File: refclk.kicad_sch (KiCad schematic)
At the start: 57 parts, among them J10 U.FL-R, Q1 PMOS Si2343DS, Q2 MMBT3904, Q3 PMOS Si2343DS, U14 LP5907MFX-3.3, U16 TLV3501, U18 NC7SV157, U19 74LVC2G14, U20 Si5351A, U21 NC7SV157, U22 SN65LVDS1, X1 TCXO-27M

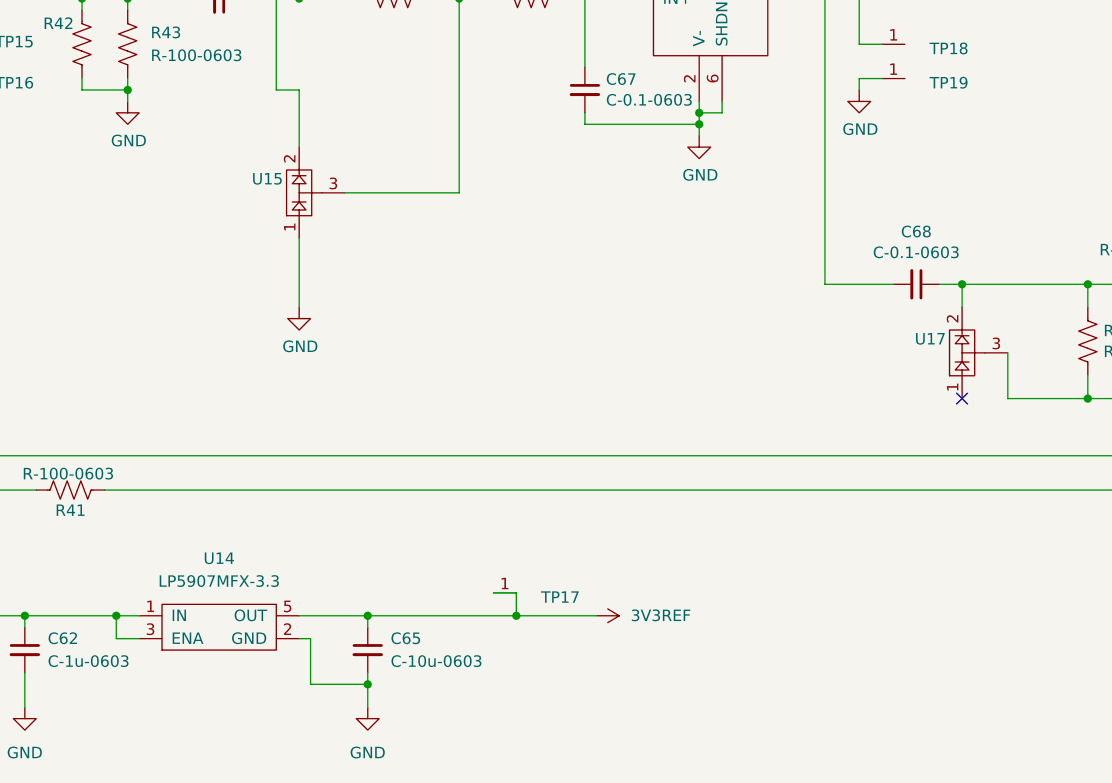
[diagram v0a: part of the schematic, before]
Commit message: Bring over ringof/dev: design + 3D + mechanical/viewer + CI (#58)
* throwaway: exercise design -> dev pipeline (safe to delete)

* Bring over ringof/dev (tranche 2, stage 1): design, library, 3D, board CI & docs

* Bring over ringof/dev (tranche 2, stage 2): mechanical enclosure + 3D viewer

* run_checks: hard-fail the 3D-model check regardless of ENFORCE

* Improved 3D viewer (#59)

* mechanical: give the end plates a Blue soldermask stackup

The end-plate PCBs had no physical stackup, so KiCad exported them with the
default green soldermask. Add a 2-layer stackup with front/back mask set to the
named "Blue" preset, summing to the existing 1.6 mm so board thickness / fit is
unchanged. This makes the plates export blue-dominant so the viewer's soldermask
recolour treats them the same as the main board.

* feat(viewer): part toggles, upright orientation, Turn Island navy, even lighting

Grow the mechanical fit-check viewer into an interactive, correctly-coloured one:

- Part toggles: show/hide enclosure, main board, front/rear end plate. Rebuilt on
  pinned three.js r148 (model-viewer has no per-node visibility API); a checkbox
  flips object.visible on each part's prefixed nodes. Libraries inlined via a
  runtime import map -- no bundler, fully offline.
- Upright orientation (180 deg roll), click-to-set-pivot, and a header showing the
  git hash and branch as links (new --repo-url, fed from the CI environment).
- Board colour: assemble_glb recolours the blue soldermask to the Turn Island navy
  (KiCad's "Blue" preset exports a brighter cornflower); detection targets only the
  matte, blue-dominant mask material. The material is identical on every face, so
  the viewer lighting is set to an orientation-independent rig (soft key + strong
  ambient + damped environment) so every face reads the same navy.
- Checkbox reload-sync: autocomplete="off" + re-apply each box's state on load so
  the model always matches the checkboxes after a refresh.

Colour is applied downstr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
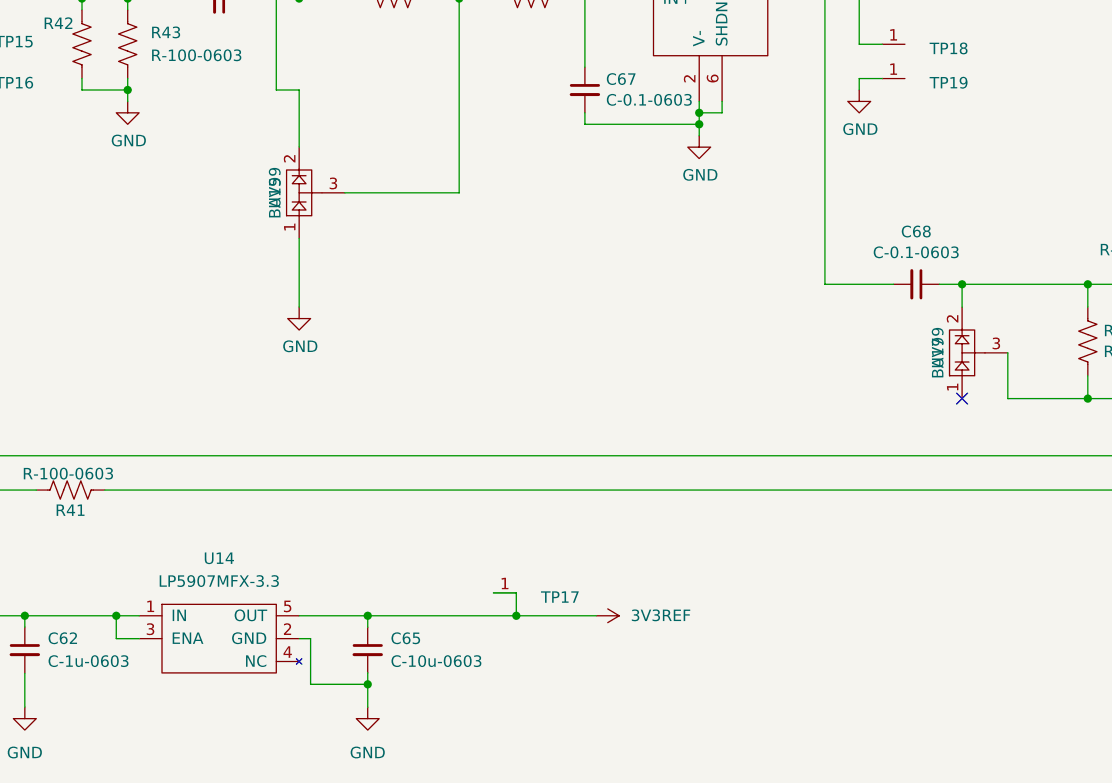
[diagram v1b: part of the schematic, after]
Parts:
- C62, C65: footprint TIS_Footprints:PAD_0603 -> Library:C_0603
- C63, C64, C66, C67, C68, C69, C70, C71, C72, C73, C74, C75, C76: footprint TIS_Footprints:C_0603 -> Library:C_0603
- C78: footprint TIS_Footprints:PAD_0603 -> Library:C_0603; symbol capacitors:C-8.2p-0603 -> Library:C-8.2p-0603
- J10: footprint TIS_Footprints:HRS_U.FL-R-SMT(01) -> Library:HRS_U.FL-R-SMT(01)
- L15, L16, L17: footprint TIS_Footprints:0603 -> Library:0603
- Q1, Q2, Q3: footprint TIS_Footprints:SOT-23 -> Library:SOT-23
- R41, R42, R43, R44, R45, R46, R47, R48, R49, R50, R51, R52, R53, R54, R55, R56, R57, R60: footprint TIS_Footprints:PAD_0603 -> Library:PAD_0603
- R61: footprint TIS_Footprints:PAD_0603 -> Library:PAD_0603; symbol resistors:R-100-0603 -> Library:R-100-0603
- TP15, TP16, TP17, TP18, TP19: footprint TIS_Footprints:TP -> Library:TP
- U14, U22: footprint TIS_Footprints:SOT-23-5 -> Library:SOT-23-5
- U15, U17: value (none) -> BAV99; footprint TIS_Footprints:SOT-23 -> Library:SOT-23
- U16: footprint TIS_Footprints:SOT-23-6 -> Library:SOT-23-6
- U18, U21: footprint TIS_Footprints:SC-70-6 -> Library:SC-70-6
- U19: footprint TIS_Footprints:SC-70-6_rot90 -> Library:SC-70-6_rot90
- U20: footprint TIS_Footprints:MSOP-10_W3mm -> Library:MSOP-10_W3mm
- X1: footprint TIS_Footprints:TCXO-3225 -> Library:TCXO-3225; Comment alternate: C46598427 ±2ppm -> (none)

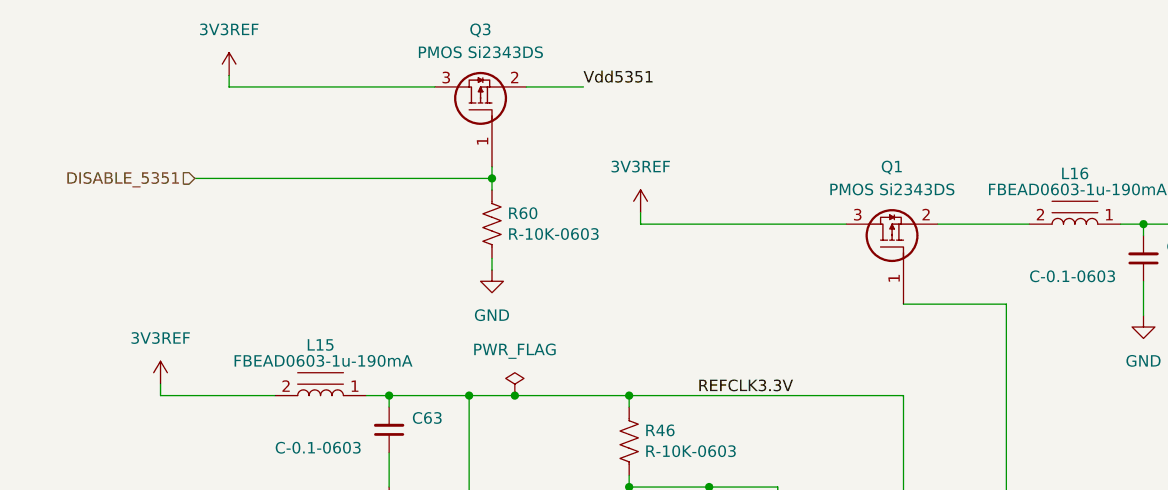
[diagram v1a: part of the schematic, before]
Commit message: Q1/Q3 D/S swap, TP11, TP12 to TPTiny and relocate
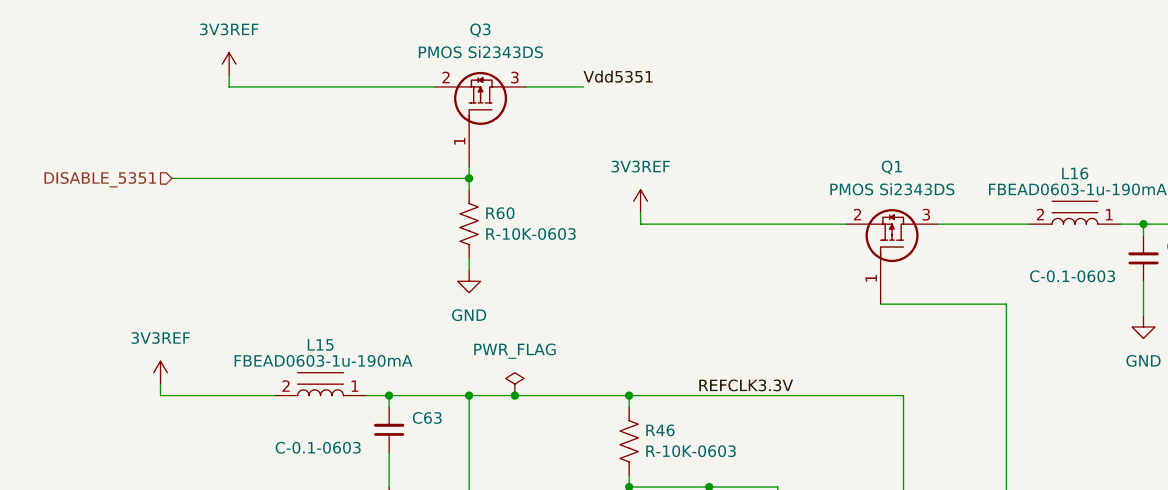
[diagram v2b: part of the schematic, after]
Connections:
- net 3V3REF: now also Q1.2 (S), Q3.2 (S); no longer Q1.3 (D), Q3.3 (D)
- net Vdd5351: now also Q3.3 (D); no longer Q3.2 (S)
- net at L16.2: now also Q1.3 (D); no longer Q1.2 (S)
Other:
- moved on the sheet: Q1, Q3, R60
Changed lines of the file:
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@@
 	)
 	(junction
-		(at 63.5 31.75)
+		(at 60.96 31.75)
 		(diameter 0)
 		(color 0 0 0 0)
@@
 	(wire
 		(pts
-			(xy 63.5 31.75) (xy 63.5 33.02)
+			(xy 60.96 31.75) (xy 60.96 33.02)
 		)
 		(stroke
@@
 	(wire
 		(pts
-			(xy 120.65 45.72) (xy 109.22 45.72)
-		)
-		(stroke
-			(width 0)
-			(type default)
-		)
-	)
-	(wire
-		(pts
 			(xy 146.05 36.83) (xy 146.05 64.77)
 		)
@@
 	(wire
 		(pts
+			(xy 106.68 45.72) (xy 120.65 45.72)
+		)
+		(stroke
+			(width 0)
+			(type default)
+		)
+	)
+	(wire
+		(pts
 			(xy 248.92 138.43) (xy 248.92 130.81)
 		)
@@
 	(wire
 		(pts
-			(xy 63.5 30.48) (xy 63.5 31.75)
+			(xy 60.96 30.48) (xy 60.96 31.75)
 		)
 		(stroke
@@
 	(wire
 		(pts
-			(xy 63.5 40.64) (xy 63.5 41.91)
+			(xy 60.96 40.64) (xy 60.96 41.91)
 		)
 		(stroke
@@
 	(wire
 		(pts
-			(xy 30.48 31.75) (xy 63.5 31.75)
+			(xy 27.94 31.75) (xy 60.96 31.75)
 		)
 		(stroke
@@
 	(hierarchical_label "DISABLE_5351"
 		(shape input)
-		(at 30.48 31.75 180)
+		(at 27.94 31.75 180)
 		(effects
 			(font
@@
 	(symbol
 		(lib_id "Library:PMOS Si2343DS")
-		(at 107.95 39.37 90)
+		(at 107.95 39.37 270)
+		(mirror x)
 		(unit 1)
 		(body_style 1)
@@
 		(in_pos_files yes)
 		(dnp no)
-		(fields_autoplaced yes)
 		(property "Reference" "Q1"
 			(at 107.95 30.48 90)
@@
 		)
 		(property "Footprint" "Library:SOT-23"
-			(at 109.855 34.29 0)
+			(at 106.045 34.29 0)
 			(hide yes)
 			(show_name no)
@@
 		)
 		(property "LCSC Part #" "C6903"
-			(at 104.14 34.29 0)
+			(at 111.76 34.29 0)
 			(hide yes)
 			(show_name no)
@@
 	(symbol
 		(lib_id "Library:GND")
-		(at 63.5 41.91 0)
+		(at 60.96 41.91 0)
 		(unit 1)
 		(body_style 1)
@@
 		(fields_autoplaced yes)
 		(property "Reference" "#PWR0107"
-			(at 63.5 48.26 0)
+			(at 60.96 48.26 0)
 			(hide yes)
 			(show_name no)
@@
 		)
 		(property "Value" "GND"
-			(at 63.5 46.99 0)
+			(at 60.96 46.99 0)
 			(show_name no)
 			(do_not_autoplace no)
@@
 		)
 		(property "Footprint" ""
-			(at 63.5 41.91 0)
+			(at 60.96 41.91 0)
 			(hide yes)
 			(show_name no)
@@
 		)
 		(property "Datasheet" ""
-			(at 63.5 41.91 0)
+			(at 60.96 41.91 0)
 			(hide yes)
 			(show_name no)
@@
 		)
 		(property "Description" ""
-			(at 63.5 41.91 0)
+			(at 60.96 41.91 0)
 			(hide yes)
 			(show_name no)
@@
 		)
 		(property "LCSC Part #" ""
-			(at 63.5 41.91 0)
+			(at 60.96 41.91 0)
 			(hide yes)
 			(show_name no)
@@
 	(symbol
 		(lib_id "Library:R-10K-0603")
-		(at 63.5 36.83 0)
+		(at 60.96 36.83 0)
 		(unit 1)
 		(body_style 1)
@@
 		(dnp no)
 		(property "Reference" "R60"
-			(at 65.2272 35.6616 0)
+			(at 62.6872 35.6616 0)
 			(show_name no)
 			(do_not_autoplace no)
@@
 		)
 		(property "Value" "R-10K-0603"
-			(at 65.2272 37.973 0)
+			(at 62.6872 37.973 0)
 			(show_name no)
 			(do_not_autoplace no)
@@
 		)
 		(property "Footprint" "Library:PAD_0603"
-			(at 64.516 37.084 90)
+			(at 61.976 37.084 90)
 			(hide yes)
 			(show_name no)
@@
 		)
 		(property "Datasheet" ""
-			(at 63.5 36.83 0)
+			(at 60.96 36.83 0)
 			(hide yes)
 			(show_name no)
@@
 		)
 		(property "Description" ""
-			(at 63.5 36.83 0)
+			(at 60.96 36.83 0)
 			(hide yes)
 			(show_name no)
@@
 		)
 		(property "LCSC Part #" "C25804"
-			(at 63.5 36.83 0)
+			(at 60.96 36.83 0)
 			(hide yes)
 			(show_name no)
@@
 	(symbol
 		(lib_id "Library:PMOS Si2343DS")
-		(at 62.23 24.13 90)
+		(at 62.23 24.13 270)
+		(mirror x)
 		(unit 1)
 		(body_style 1)
@@
 		(in_pos_files yes)
 		(dnp no)
-		(fields_autoplaced yes)
 		(property "Reference" "Q3"
 			(at 62.23 15.24 90)
@@
 		)
 		(property "Footprint" "Library:SOT-23"
-			(at 64.135 19.05 0)
+			(at 60.325 19.05 0)
 			(hide yes)
 			(show_name no)
@@
 		)
 		(property "LCSC Part #" "C6903"
-			(at 58.42 19.05 0)
+			(at 66.04 19.05 0)
 			(hide yes)
 			(show_name no)
